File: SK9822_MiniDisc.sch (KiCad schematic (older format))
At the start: 333 parts, among them P1 CONN_01X04, P2 CONN_01X04

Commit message: further signal line tweaks
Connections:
- net GND: now also P1.1 (P1), P2.1 (P1); no longer P1.4 (P4), P2.4 (P4)
- net VCC: now also P1.4 (P4), P2.4 (P4); no longer P1.1 (P1), P2.1 (P1)
- net at D1.1 (DIN): now also P1.3 (P3); no longer P1.2 (P2)
- net at D1.2 (CIN): now also P1.2 (P2); no longer P1.3 (P3)
- net at D331.5 (COUT): now also P2.2 (P2); no longer P2.3 (P3)
- net at D331.6 (DOUT): now also P2.3 (P3); no longer P2.2 (P2)
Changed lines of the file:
@@
 LIBS:valves
 LIBS:apa102_sk9822
+LIBS:SK9822_MiniDisc-cache
 EELAYER 25 0
 EELAYER END
@@
 F 3 "" H 1300 2250 50  0000 C CNN
 	1    1300 2250
-	-1   0    0    -1
+	-1   0    0    1
 $EndComp
 Text GLabel 1500 2100 2    60   Input ~ 0
@@
 F 3 "" H 4700 22850 50  0000 C CNN
 	1    4700 22850
-	1    0    0    -1
+	1    0    0    1
 $EndComp
 Text GLabel 4500 22700 0    60   Input ~ 0

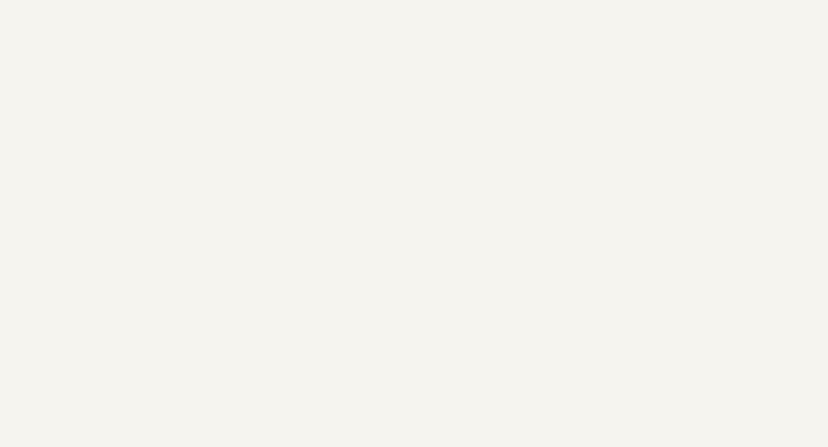
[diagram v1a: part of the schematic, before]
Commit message: adding caps
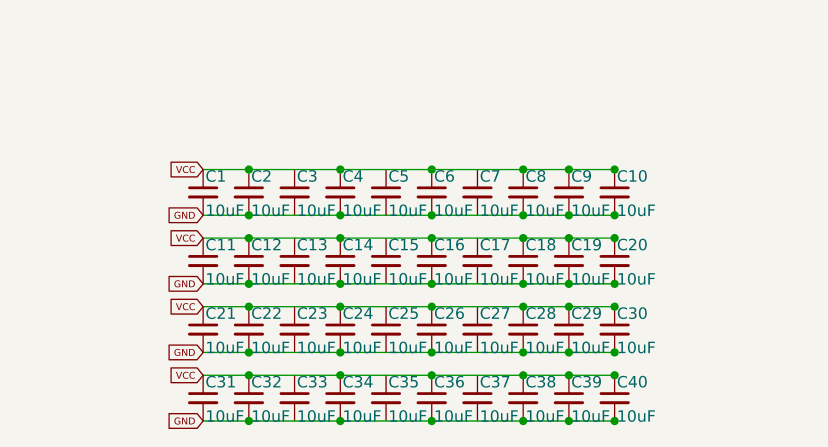
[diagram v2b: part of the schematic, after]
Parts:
- added C1, C10, C11, C12, C13, C14, C15, C16, C17, C18, C19, C2, C20, C21, C22, C23, C24, C25, C26, C27, C28, C29, C3, C30, C31, C32, C33, C34, C35, C36, C37, C38, C39, C4, C40, C5, C6, C7, C8, C9: 10uF, Capacitors_SMD:C_0805, symbol C_Small
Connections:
- net GND: now also C1.2, C10.2, C11.2, C12.2, C14.2, C16.2, C18.2, C19.2, C2.2, C20.2, C21.2, C22.2, C24.2, C26.2, C28.2, C29.2, C30.2, C31.2, C32.2, C34.2, C36.2, C38.2, C39.2, C4.2, C40.2, C6.2, C8.2, C9.2
- net VCC: now also C1.1, C10.1, C11.1, C12.1, C14.1, C16.1, C18.1, C19.1, C2.1, C20.1, C21.1, C22.1, C24.1, C26.1, C28.1, C29.1, C30.1, C31.1, C32.1, C34.1, C36.1, C38.1, C39.1, C4.1, C40.1, C6.1, C8.1, C9.1

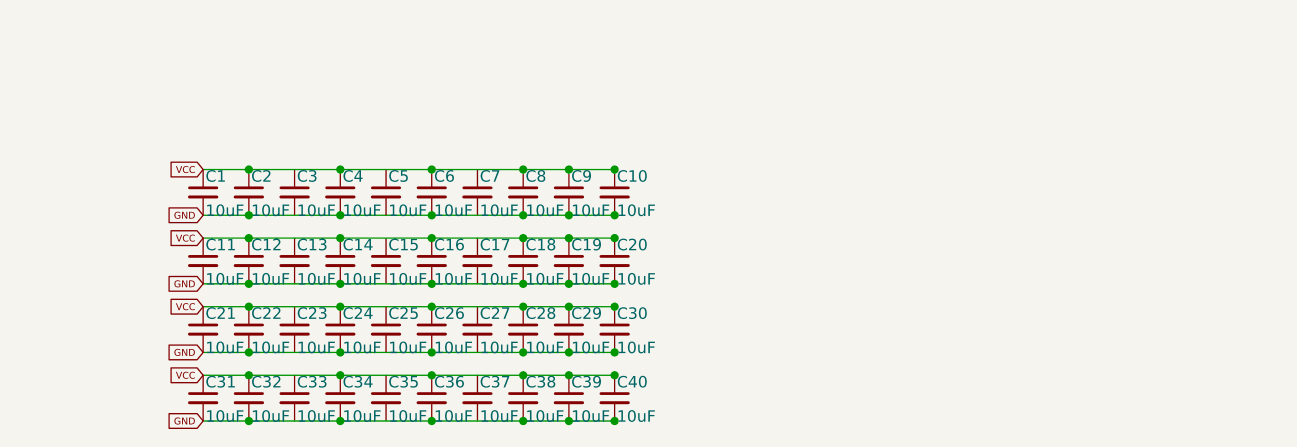
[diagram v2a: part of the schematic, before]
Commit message: places caps
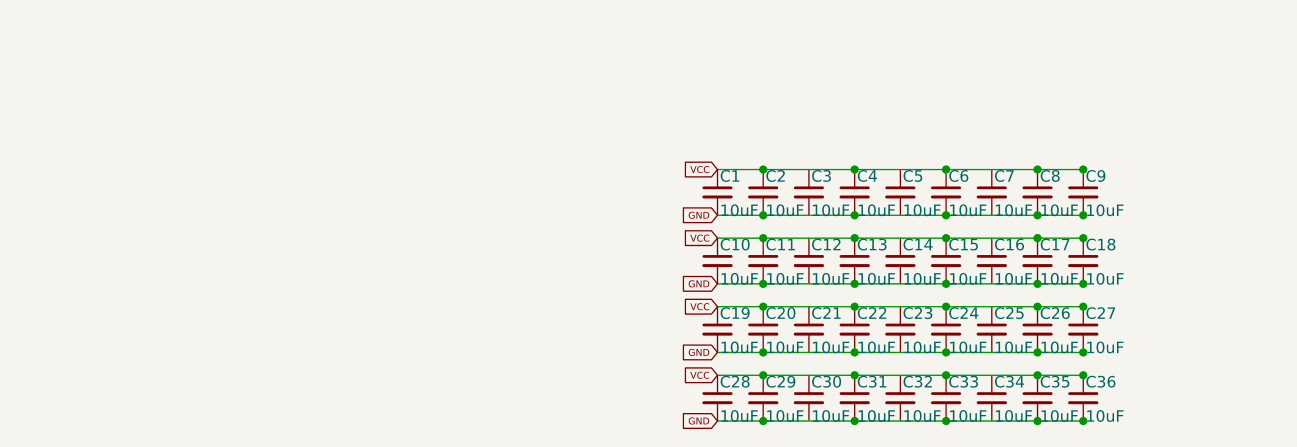
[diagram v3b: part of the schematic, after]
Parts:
- removed C37, C38, C39, C40: 10uF, Capacitors_SMD:C_0805, symbol C_Small
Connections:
- net GND: now also C13.2, C15.2, C17.2, C27.2, C33.2, C35.2; no longer C12.2, C14.2, C16.2, C21.2, C30.2, C32.2, C34.2
- net VCC: now also C13.1, C15.1, C17.1, C27.1, C33.1, C35.1; no longer C12.1, C14.1, C16.1, C21.1, C30.1, C32.1, C34.1

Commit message: finaly got caps right
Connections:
- net GND: now also C12.2, C14.2, C16.2, C21.2, C23.2, C25.2, C3.2, C30.2, C32.2, C34.2, C5.2, C7.2
- net VCC: now also C12.1, C14.1, C16.1, C21.1, C23.1, C25.1, C3.1, C30.1, C32.1, C34.1, C5.1, C7.1
